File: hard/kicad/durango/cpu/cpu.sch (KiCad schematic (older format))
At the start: 34 parts, among them J1 NANOLINK, J2 IO9 INPUT, J3 IO8 PORT, Q1 BC547, Q2 BC547, Q3 BC547, SW1 RESET, U1 65SC02, U10 4040, U11 74HC30, U12 LTC4622G, U2 62256, U3 27C128, U4 74HC139, U5 74HC139, U6 74HC139, U7 74HC374, U8 74HC74, U9 74HC245, X1 1 MHz

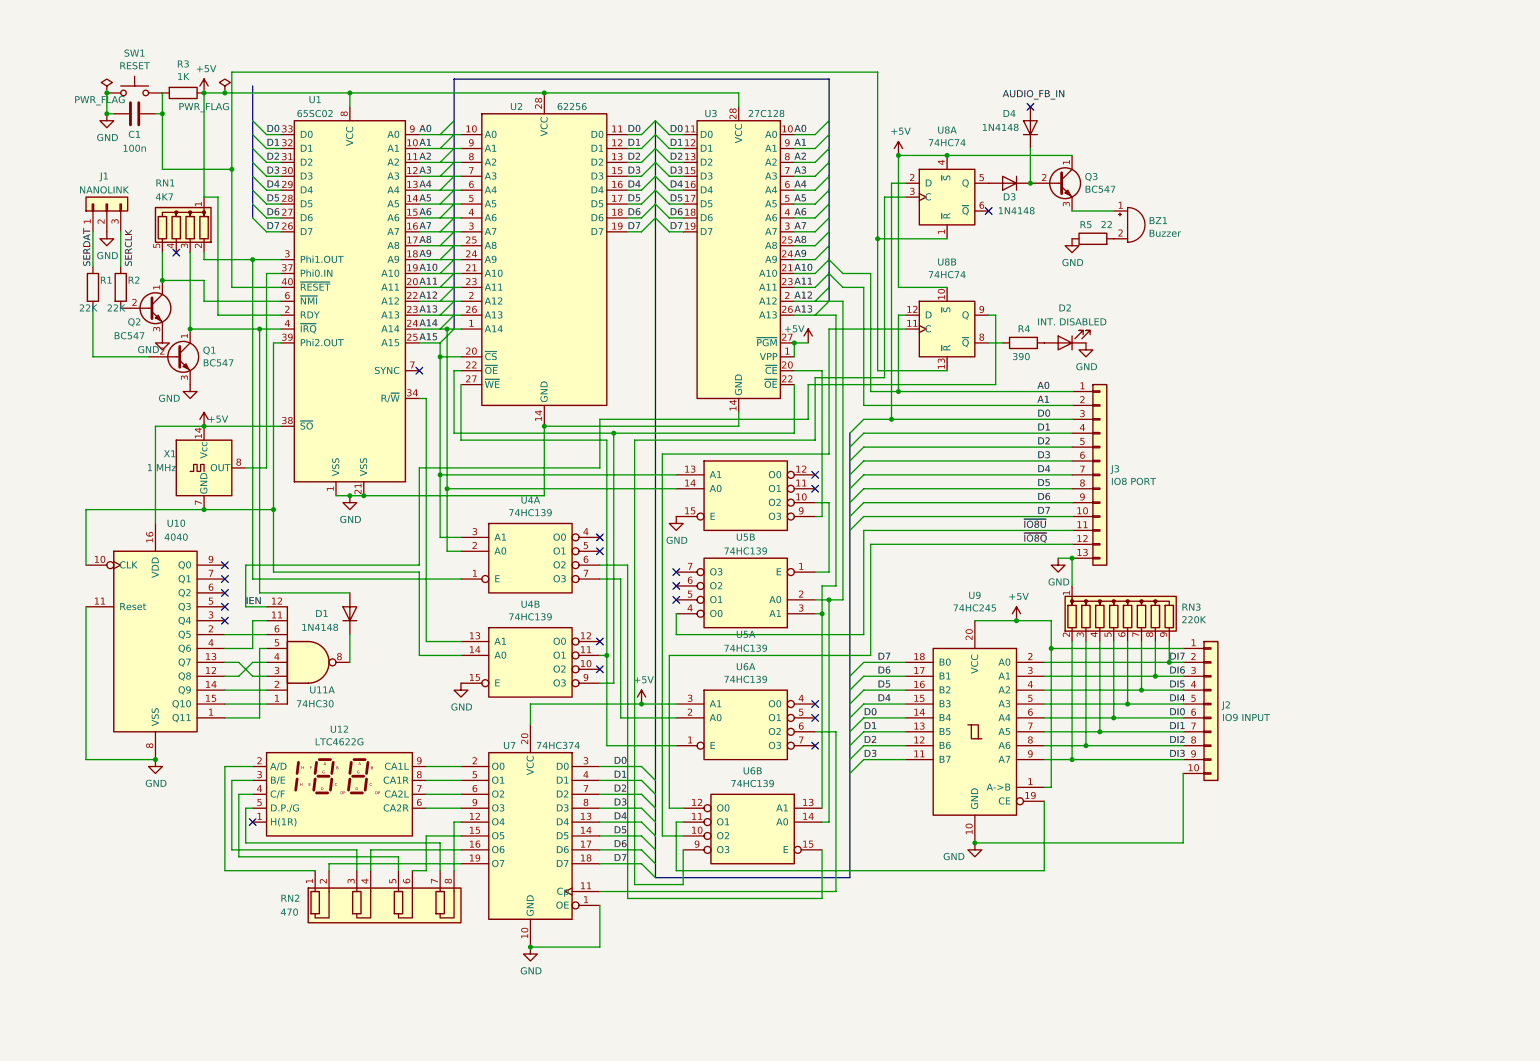
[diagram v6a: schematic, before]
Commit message: fixed power pins in Durango sch
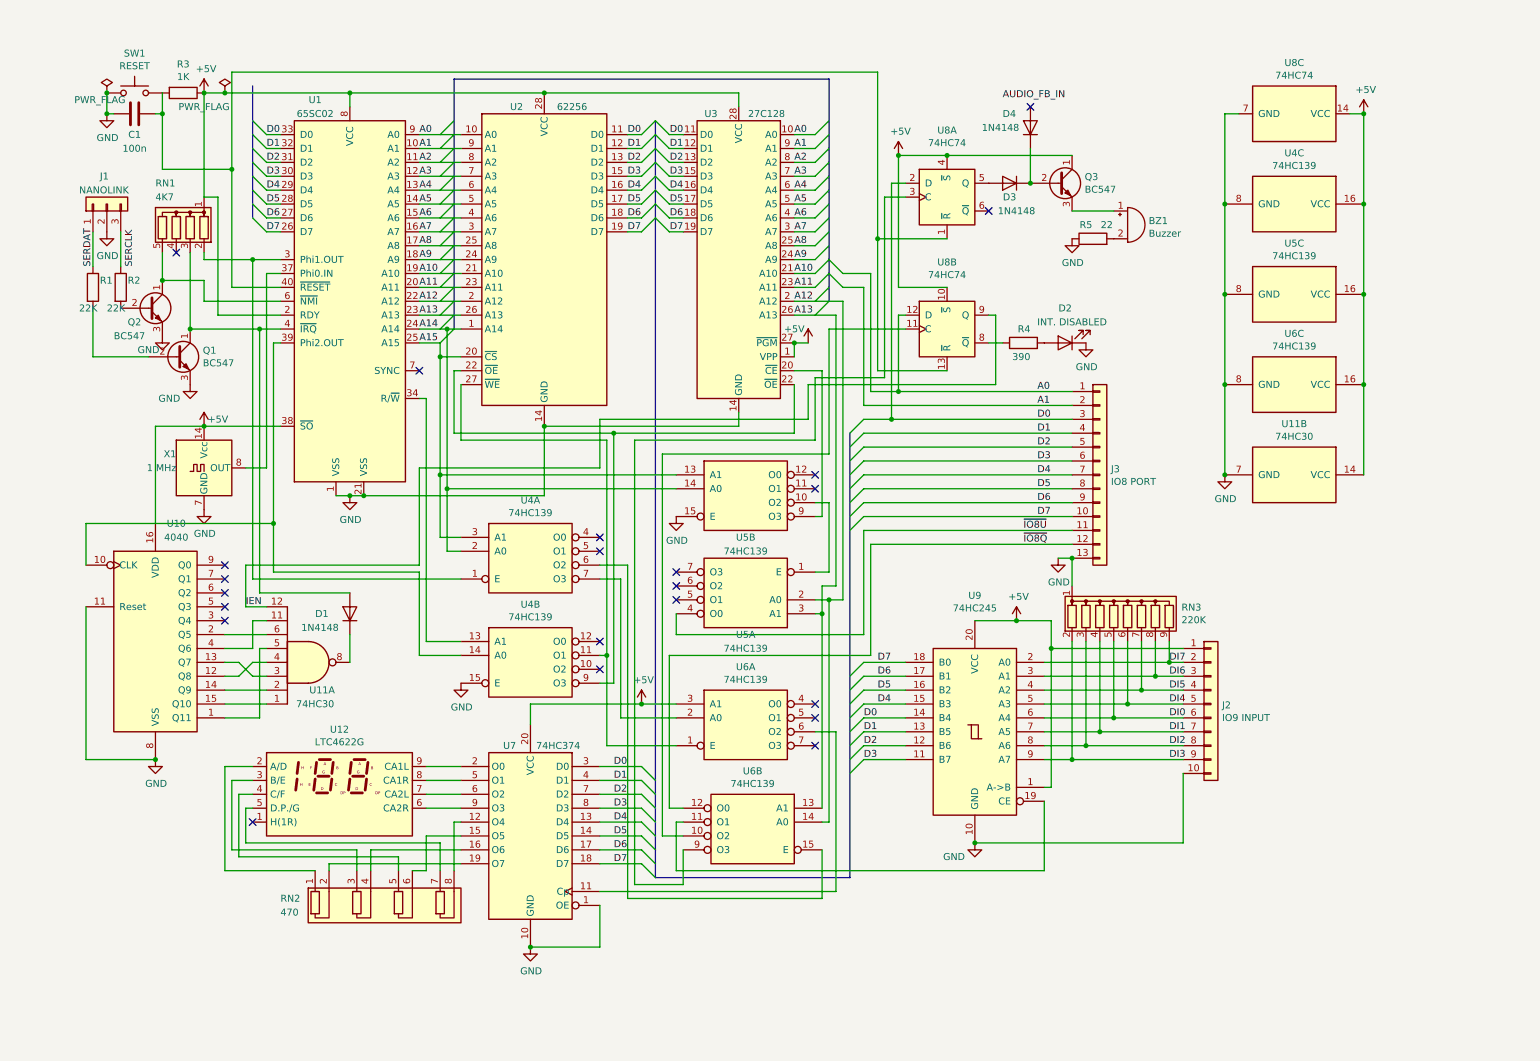
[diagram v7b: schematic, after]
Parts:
- added unit 2 of U11
- added unit 3 of U4
- added unit 3 of U5
- added unit 3 of U6
- added unit 3 of U8
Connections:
- net +5V: now also U11.14 (VCC), U4.16 (VCC), U5.16 (VCC), U6.16 (VCC), U8.14 (VCC)
- net GND: now also X1.7 (GND), U11.7 (GND), U4.8 (GND), U5.8 (GND), U6.8 (GND), U8.7 (GND)
- net at U1.39 (Phi2.OUT), U10.10 (CLK), U4.14 (A0): no longer X1.7 (GND)
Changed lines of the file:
@@
 	1950 2650 1900 2650
 Wire Wire Line
-	1900 2650 1900 3850
-Wire Wire Line
-	550  4250 550  3850
-Wire Wire Line
-	550  3850 1400 3850
+	1900 2650 1900 3950
+Wire Wire Line
+	550  4250 550  3950
 $Comp
 L cpu-rescue:BC547-Transistor_BJT-cpu-rescue-cpu-rescue-cpu-rescue Q1
@@
 	5850 2850 5650 2850
 Wire Wire Line
-	1900 3850 1900 4300
+	1900 3950 1900 4300
 Wire Wire Line
 	1900 4300 2950 4300
@@
 Wire Wire Line
 	2950 4900 3250 4900
-Connection ~ 1900 3850
+Connection ~ 1900 3950
 Wire Wire Line
 	2950 3050 3000 3050
@@
 	1    0    0    -1
 $EndComp
-Connection ~ 1400 3850
-Wire Wire Line
-	1400 3850 1900 3850
 Wire Wire Line
 	1950 3250 1400 3250
@@
 Wire Wire Line
 	1550 5700 1750 5700
+Wire Bus Line
+	3200 750  3200 2550
+Wire Wire Line
+	550  3950 1900 3950
+$Comp
+L power:GND #PWR0115
+U 1 1 608F0193
+P 1400 3850
+F 0 "#PWR0115" H 1400 3600 50  0001 C CNN
+F 1 "GND" H 1405 3677 50  0000 C CNN
+F 2 "" H 1400 3850 50  0001 C CNN
+F 3 "" H 1400 3850 50  0001 C CNN
+	1    1400 3850
+	1    0    0    -1
+$EndComp
+$Comp
+L 74xx:74HC74 U8
+U 3 1 60907796
+P 9250 1000
+F 0 "U8" V 8883 1000 50  0000 C CNN
+F 1 "74HC74" V 8974 1000 50  0000 C CNN
+F 2 "" H 9250 1000 50  0001 C CNN
+F 3 "74xx/74hc_hct74.pdf" H 9250 1000 50  0001 C CNN
+	3    9250 1000
+	0    1    1    0
+$EndComp
+$Comp
+L 74xx:74LS139 U4
+U 3 1 6090C838
+P 9250 1650
+F 0 "U4" V 8883 1650 50  0000 C CNN
+F 1 "74HC139" V 8974 1650 50  0000 C CNN
+F 2 "" H 9250 1650 50  0001 C CNN
+F 3 "http://www.ti.com/lit/gpn/sn74LS139" H 9250 1650 50  0001 C CNN
+	3    9250 1650
+	0    1    1    0
+$EndComp
+$Comp
+L 74xx:74LS139 U5
+U 3 1 6090D89D
+P 9250 2300
+F 0 "U5" V 8883 2300 50  0000 C CNN
+F 1 "74HC139" V 8974 2300 50  0000 C CNN
+F 2 "" H 9250 2300 50  0001 C CNN
+F 3 "http://www.ti.com/lit/gpn/sn74LS139" H 9250 2300 50  0001 C CNN
+	3    9250 2300
+	0    1    1    0
+$EndComp
+$Comp
+L 74xx:74LS139 U6
+U 3 1 6090E3CA
+P 9250 2950
+F 0 "U6" V 8883 2950 50  0000 C CNN
+F 1 "74HC139" V 8974 2950 50  0000 C CNN
+F 2 "" H 9250 2950 50  0001 C CNN
+F 3 "http://www.ti.com/lit/gpn/sn74LS139" H 9250 2950 50  0001 C CNN
+	3    9250 2950
+	0    1    1    0
+$EndComp
+$Comp
+L 74xx:74LS30 U11
+U 2 1 6091DC27
+P 9250 3600
+F 0 "U11" V 8883 3600 50  0000 C CNN
+F 1 "74HC30" V 8974 3600 50  0000 C CNN
+F 2 "" H 9250 3600 50  0001 C CNN
+F 3 "http://www.ti.com/lit/gpn/sn74LS30" H 9250 3600 50  0001 C CNN
+	2    9250 3600
+	0    1    1    0
+$EndComp
+Wire Wire Line
+	8750 3600 8750 2950
+Wire Wire Line
+	8750 1000 8850 1000
+Connection ~ 8750 1650
+Wire Wire Line
+	8750 1650 8750 1000
+Connection ~ 8750 2300
+Wire Wire Line
+	8750 2300 8750 1650
+Connection ~ 8750 2950
+Wire Wire Line
+	8750 2950 8750 2300
+Wire Wire Line
+	9650 1000 9750 1000
+Wire Wire Line
+	9750 1000 9750 1650
 Wire Wire Line
 	5650 2450 5950 2450
@@
 Wire Bus Line
 	4650 1050 4650 6500
-Wire Bus Line
-	3200 750  3200 2550
+Connection ~ 9750 1650
+Wire Wire Line
+	9750 1650 9750 2300
+Connection ~ 9750 2300
+Wire Wire Line
+	9750 2300 9750 2950
+Connection ~ 9750 2950
+Wire Wire Line
+	9750 2950 9750 3600
+$Comp
+L power:GND #PWR?
+U 1 1 6097CD4D
+P 8750 3600
+F 0 "#PWR?" H 8750 3350 50  0001 C CNN
+F 1 "GND" H 8755 3427 50  0000 C CNN
+F 2 "" H 8750 3600 50  0001 C CNN
+F 3 "" H 8750 3600 50  0001 C CNN
+	1    8750 3600
+	1    0    0    -1
+$EndComp
+Connection ~ 8750 3600
+$Comp
+L power:+5V #PWR?
+U 1 1 60980E31
+P 9750 1000
+F 0 "#PWR?" H 9750 850 50  0001 C CNN
+F 1 "+5V" H 9765 1173 50  0000 C CNN
+F 2 "" H 9750 1000 50  0001 C CNN
+F 3 "" H 9750 1000 50  0001 C CNN
+	1    9750 1000
+	1    0    0    -1
+$EndComp
+Connection ~ 9750 1000
 $EndSCHEMATC
